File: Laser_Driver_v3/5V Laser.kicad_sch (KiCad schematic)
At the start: 19 parts, among them U11 LT3045EDD 5V, U13 LT3045EDD 5V, U17 LM7812_TO220, U5 LM7808_TO220

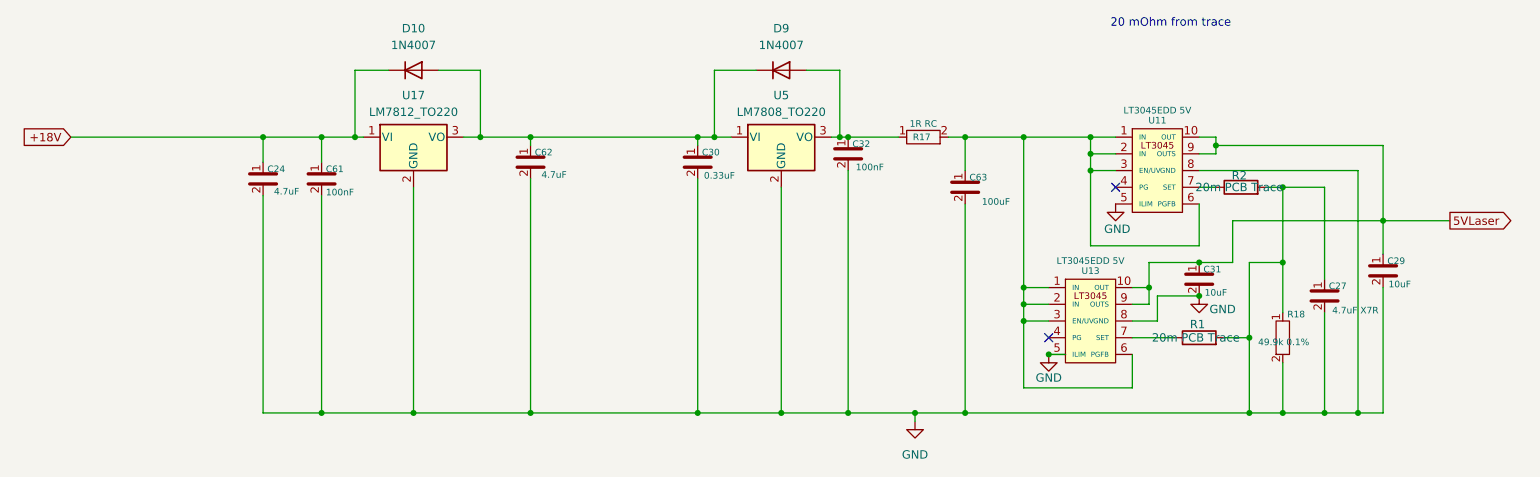
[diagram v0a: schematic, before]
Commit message: Renumbered schematics, corrections, power verified
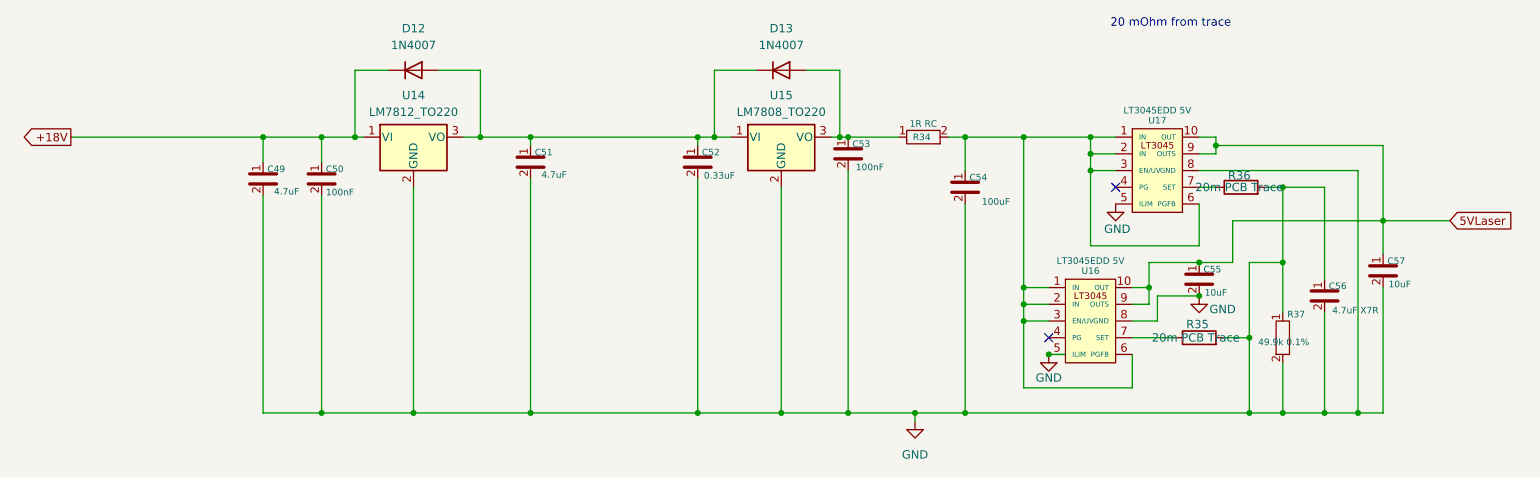
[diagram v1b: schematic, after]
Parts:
- renumbered C24 to C49, C61 to C50, C62 to C51, C30 to C52, C32 to C53, C63 to C54, C31 to C55, C27 to C56, C29 to C57, D10 to D12, D9 to D13, R17 to R34, R1 to R35, R2 to R36, R18 to R37, U17 to U14, U5 to U15, U13 to U16, U11 to U17
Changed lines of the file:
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@@
 	)
 	(global_label "5VLaser"
-		(shape output)
+		(shape input)
 		(at 248.92 54.61 0)
 		(fields_autoplaced yes)
@@
 	)
 	(global_label "+18V"
-		(shape input)
+		(shape output)
 		(at 39.37 41.91 180)
 		(fields_autoplaced yes)
@@
 		(dnp no)
 		(fields_autoplaced yes)
-		(property "Reference" "D10"
+		(property "Reference" "D12"
 			(at 91.44 25.4 0)
 			(show_name no)
@@
 			(project "laser_driver_v3"
 				(path "/b2c3d4e5-f6a7-8901-bcde-f12345678901/4c904a9b-f13b-4762-ac7d-2743bb4f9a22"
-					(reference "D10")
+					(reference "D12")
 					(unit 1)
 				)
@@
 		(in_pos_files yes)
 		(dnp no)
-		(property "Reference" "#PWR07"
+		(property "Reference" "#PWR015"
 			(at 198.12 58.42 0)
 			(hide yes)
@@
 			(project "laser_driver_v3"
 				(path "/b2c3d4e5-f6a7-8901-bcde-f12345678901/4c904a9b-f13b-4762-ac7d-2743bb4f9a22"
-					(reference "#PWR07")
+					(reference "#PWR015")
 					(unit 1)
 				)
@@
 		(dnp no)
 		(fields_autoplaced yes)
-		(property "Reference" "U17"
+		(property "Reference" "U14"
 			(at 91.44 35.56 0)
 			(show_name no)
@@
 			(project "laser_driver_v3"
 				(path "/b2c3d4e5-f6a7-8901-bcde-f12345678901/4c904a9b-f13b-4762-ac7d-2743bb4f9a22"
-					(reference "U17")
+					(reference "U14")
 					(unit 1)
 				)
@@
 		(in_pos_files yes)
 		(dnp no)
-		(property "Reference" "U13"
+		(property "Reference" "U16"
 			(at 194.31 62.23 0)
 			(show_name no)
@@
 			(project "laser_driver_v3"
 				(path "/b2c3d4e5-f6a7-8901-bcde-f12345678901/4c904a9b-f13b-4762-ac7d-2743bb4f9a22"
-					(reference "U13")
+					(reference "U16")
 					(unit 1)
 				)
@@
 		(in_pos_files yes)
 		(dnp no)
-		(property "Reference" "C24"
+		(property "Reference" "C49"
 			(at 70.58 46.76 0)
 			(show_name no)
@@
 			(project "laser_driver_v3"
 				(path "/b2c3d4e5-f6a7-8901-bcde-f12345678901/4c904a9b-f13b-4762-ac7d-2743bb4f9a22"
-					(reference "C24")
+					(reference "C49")
 					(unit 1)
 				)
@@
 		(in_pos_files yes)
 		(dnp no)
-		(property "Reference" "R18"
+		(property "Reference" "R37"
 			(at 225.552 68.834 0)
 			(show_name no)
@@
 			(project "laser_driver_v3"
 				(path "/b2c3d4e5-f6a7-8901-bcde-f12345678901/4c904a9b-f13b-4762-ac7d-2743bb4f9a22"
-					(reference "R18")
+					(reference "R37")
 					(unit 1)
 				)
@@
 		(in_pos_files yes)
 		(dnp no)
-		(property "Reference" "R1"
+		(property "Reference" "R35"
 			(at 210.566 70.358 90)
 			(show_name no)
@@
 			(project "laser_driver_v3"
 				(path "/b2c3d4e5-f6a7-8901-bcde-f12345678901/4c904a9b-f13b-4762-ac7d-2743bb4f9a22"
-					(reference "R1")
+					(reference "R35")
 					(unit 1)
 				)
@@
 		(in_pos_files yes)
 		(dnp no)
-		(property "Reference" "C62"
+		(property "Reference" "C51"
 			(at 111.22 44.22 0)
 			(show_name no)
@@
 			(project "laser_driver_v3"
 				(path "/b2c3d4e5-f6a7-8901-bcde-f12345678901/4c904a9b-f13b-4762-ac7d-2743bb4f9a22"
-					(reference "C62")
+					(reference "C51")
 					(unit 1)
 				)
@@
 		(in_pos_files yes)
 		(dnp no)
-		(property "Reference" "C63"
+		(property "Reference" "C54"
 			(at 177.26 48.03 0)
 			(show_name no)
@@
 			(project "laser_driver_v3"
 				(path "/b2c3d4e5-f6a7-8901-bcde-f12345678901/4c904a9b-f13b-4762-ac7d-2743bb4f9a22"
-					(reference "C63")
+					(reference "C54")
 					(unit 1)
 				)
@@
 		(dnp no)
 		(fields_autoplaced yes)
-		(property "Reference" "U5"
+		(property "Reference" "U15"
 			(at 147.32 35.56 0)
 			(show_name no)
@@
 			(project "laser_driver_v3"
 				(path "/b2c3d4e5-f6a7-8901-bcde-f12345678901/4c904a9b-f13b-4762-ac7d-2743bb4f9a22"
-					(reference "U5")
+					(reference "U15")
 					(unit 1)
 				)
@@
 		(in_pos_files yes)
 		(dnp no)
-		(property "Reference" "#PWR012"
+		(property "Reference" "#PWR016"
 			(at 210.82 72.39 0)
 			(hide yes)
@@
 			(project "laser_driver_v3"
 				(path "/b2c3d4e5-f6a7-8901-bcde-f12345678901/4c904a9b-f13b-4762-ac7d-2743bb4f9a22"
-					(reference "#PWR012")
+					(reference "#PWR016")
 					(unit 1)
 				)
@@
 		(in_pos_files yes)
 		(dnp no)
-		(property "Reference" "C61"
+		(property "Reference" "C50"
 			(at 79.47 46.76 0)
 			(show_name no)
@@
 			(project "laser_driver_v3"
 				(path "/b2c3d4e5-f6a7-8901-bcde-f12345678901/4c904a9b-f13b-4762-ac7d-2743bb4f9a22"
-					(reference "C61")
+					(reference "C50")
 					(unit 1)
 				)
@@
 		(in_pos_files yes)
 		(dnp no)
-		(property "Reference" "C32"
+		(property "Reference" "C53"
 			(at 159.48 42.95 0)
 			(show_name no)
@@
 			(project "laser_driver_v3"
 				(path "/b2c3d4e5-f6a7-8901-bcde-f12345678901/4c904a9b-f13b-4762-ac7d-2743bb4f9a22"
-					(reference "C32")
+					(reference "C53")
 					(unit 1)
 				)
@@
 		(in_pos_files yes)
 		(dnp no)
-		(property "Reference" "R2"
+		(property "Reference" "R36"
 			(at 216.916 47.752 90)
 			(show_name no)
@@
 			(project "laser_driver_v3"
 				(path "/b2c3d4e5-f6a7-8901-bcde-f12345678901/4c904a9b-f13b-4762-ac7d-2743bb4f9a22"
-					(reference "R2")
+					(reference "R36")
 					(unit 1)
 				)
@@
 		(dnp no)
 		(fields_autoplaced yes)
-		(property "Reference" "D9"
+		(property "Reference" "D13"
 			(at 147.32 25.4 0)
 			(show_name no)
@@
 			(project "laser_driver_v3"
 				(path "/b2c3d4e5-f6a7-8901-bcde-f12345678901/4c904a9b-f13b-4762-ac7d-2743bb4f9a22"
-					(reference "D9")
+					(reference "D13")
 					(unit 1)
 				)
@@
 		(in_pos_files yes)
 		(dnp no)
-		(property "Reference" "R17"
+		(property "Reference" "R34"
 			(at 168.656 41.91 90)
 			(show_name no)
@@
 			(project "laser_driver_v3"
 				(path "/b2c3d4e5-f6a7-8901-bcde-f12345678901/4c904a9b-f13b-4762-ac7d-2743bb4f9a22"
-					(reference "R17")
+					(reference "R34")
 					(unit 1)
 				)
@@
 		(in_pos_files yes)
 		(dnp no)
-		(property "Reference" "C30"
+		(property "Reference" "C52"
 			(at 136.62 44.22 0)
 			(show_name no)
@@
 			(project "laser_driver_v3"
 				(path "/b2c3d4e5-f6a7-8901-bcde-f12345678901/4c904a9b-f13b-4762-ac7d-2743bb4f9a22"
-					(reference "C30")
+					(reference "C52")
 					(unit 1)
 				)
@@
 		(in_pos_files yes)
 		(dnp no)
-		(property "Reference" "C27"
+		(property "Reference" "C56"
 			(at 231.87 64.54 0)
 			(show_name no)
@@
 			(project "laser_driver_v3"
 				(path "/b2c3d4e5-f6a7-8901-bcde-f12345678901/4c904a9b-f13b-4762-ac7d-2743bb4f9a22"
-					(reference "C27")
+					(reference "C56")
 					(unit 1)
 				)
@@
 		(in_pos_files yes)
 		(dnp no)
-		(property "Reference" "C29"
+		(property "Reference" "C57"
 			(at 240.76 60.73 0)
 			(show_name no)
@@
 			(project "laser_driver_v3"
 				(path "/b2c3d4e5-f6a7-8901-bcde-f12345678901/4c904a9b-f13b-4762-ac7d-2743bb4f9a22"
-					(reference "C29")
+					(reference "C57")
 					(unit 1)
 				)
@@
 		(in_pos_files yes)
 		(dnp no)
-		(property "Reference" "U11"
+		(property "Reference" "U17"
 			(at 204.47 39.37 0)
 			(show_name no)
@@
 			(project "laser_driver_v3"
 				(path "/b2c3d4e5-f6a7-8901-bcde-f12345678901/4c904a9b-f13b-4762-ac7d-2743bb4f9a22"
-					(reference "U11")
+					(reference "U17")
 					(unit 1)
 				)
@@
 		(in_pos_files yes)
 		(dnp no)
-		(property "Reference" "C31"
+		(property "Reference" "C55"
 			(at 212.82 62 0)
 			(show_name no)
@@
 			(project "laser_driver_v3"
 				(path "/b2c3d4e5-f6a7-8901-bcde-f12345678901/4c904a9b-f13b-4762-ac7d-2743bb4f9a22"
-					(reference "C31")
+					(reference "C55")
 					(unit 1)
 				)
@@
 		(in_pos_files yes)
 		(dnp no)
-		(property "Reference" "#PWR09"
+		(property "Reference" "#PWR014"
 			(at 187.96 81.28 0)
 			(hide yes)
@@
 			(project "laser_driver_v3"
 				(path "/b2c3d4e5-f6a7-8901-bcde-f12345678901/4c904a9b-f13b-4762-ac7d-2743bb4f9a22"
-					(reference "#PWR09")
+					(reference "#PWR014")
 					(unit 1)
 				)
@@
 		(dnp no)
 		(fields_autoplaced yes)
-		(property "Reference" "#PWR06"
+		(property "Reference" "#PWR013"
 			(at 167.64 91.44 0)
 			(hide yes)
@@
 			(project "laser_driver_v3"
 				(path "/b2c3d4e5-f6a7-8901-bcde-f12345678901/4c904a9b-f13b-4762-ac7d-2743bb4f9a22"
-					(reference "#PWR06")
-					(unit 1)
-				)
+					(reference "#PWR013")
+					(unit 1)
+				)
